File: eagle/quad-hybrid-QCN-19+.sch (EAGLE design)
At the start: 6 parts, among them J1 142-0701-851, J2 142-0701-851, J3 142-0701-851, U1 QCN-19D+

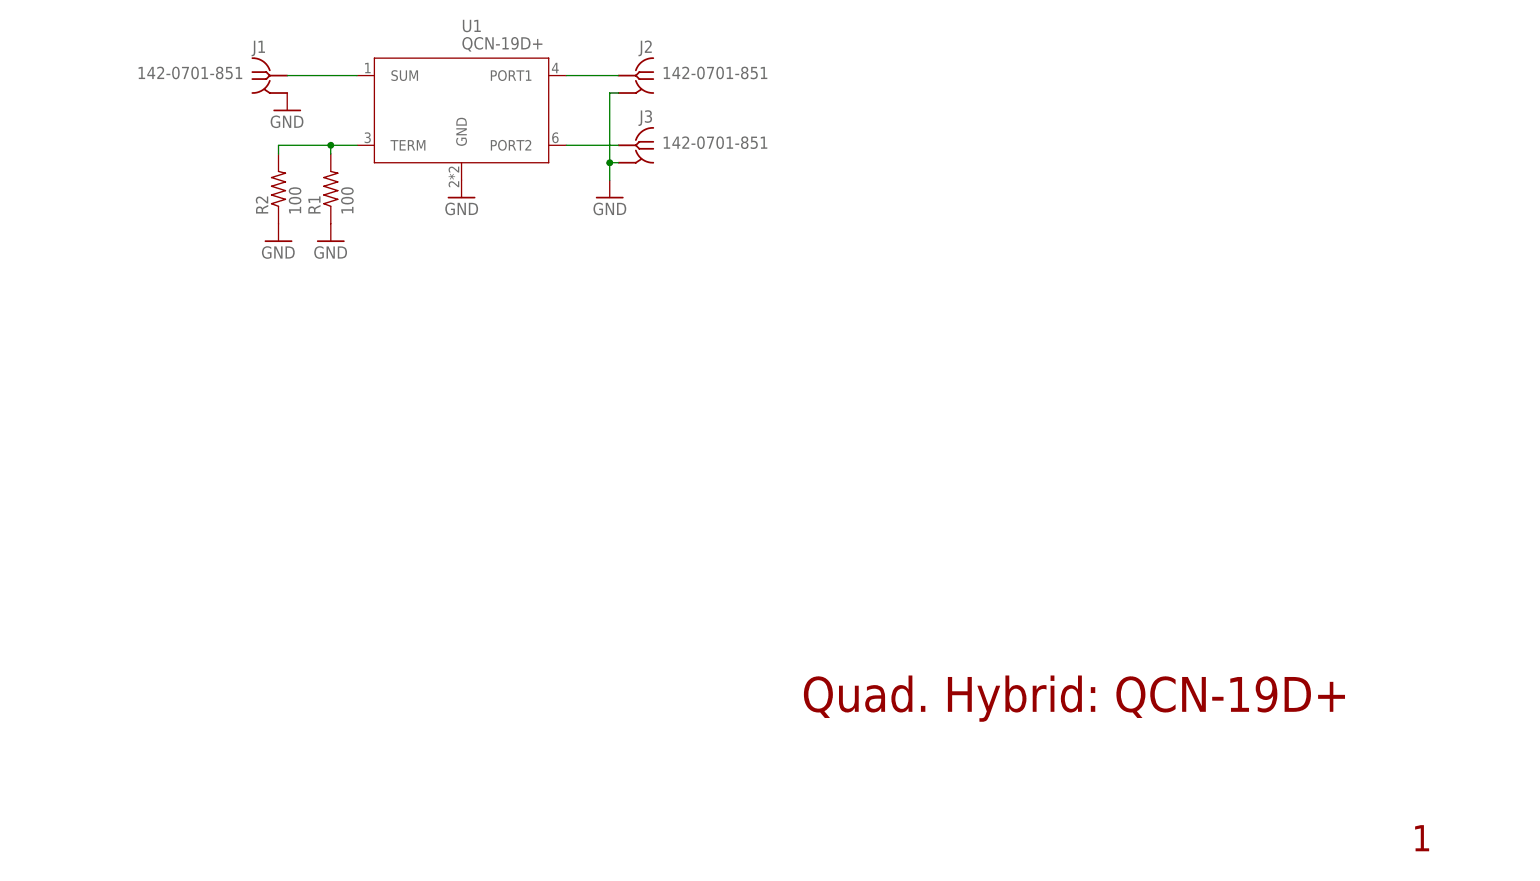
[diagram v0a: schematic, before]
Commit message: Update QCN-19+ names
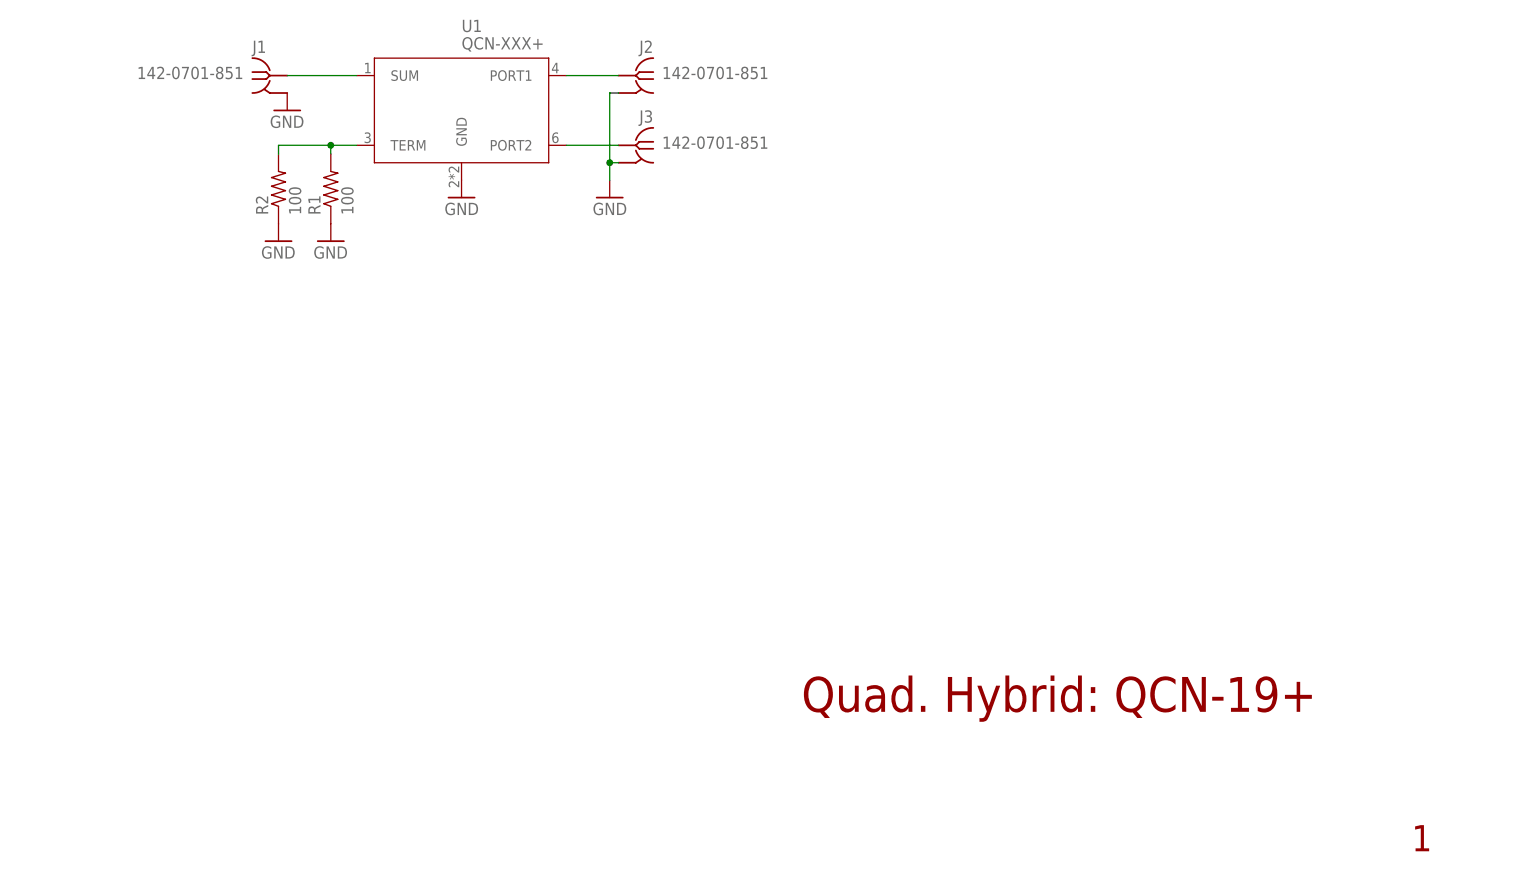
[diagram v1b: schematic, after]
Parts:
- U1: value QCN-19D+ -> QCN-XXX+; device U-MiniCirc-QCN-19+-quad:QCN-19D+ -> U-MiniCirc-QCN-XXX+-quad:QCN-XXX+
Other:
- note added: "Quad. Hybrid: QCN-19+"
- note removed: "Quad. Hybrid: QCN-19D+"
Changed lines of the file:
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@@
 <part name="GND3" library="supply1" library_urn="urn:adsk.eagle:library:371" deviceset="GND" device=""/>
 <part name="GND4" library="supply1" library_urn="urn:adsk.eagle:library:371" deviceset="GND" device=""/>
-<part name="U1" library="U-MiniCirc-QCN-19+-quad" deviceset="QCN-19D+" device=""/>
+<part name="U1" library="U-MiniCirc-QCN-XXX+-quad" deviceset="QCN-XXX+" device=""/>
 </parts>
 <sheets>
 <sheet>
 <plain>
-<text x="176.53" y="26.67" size="5.08" layer="94">Quad. Hybrid: QCN-19D+</text>
+<text x="176.53" y="26.67" size="5.08" layer="94">Quad. Hybrid: QCN-19+</text>
 <text x="265.43" y="6.35" size="3.81" layer="94">1</text>
 </plain>

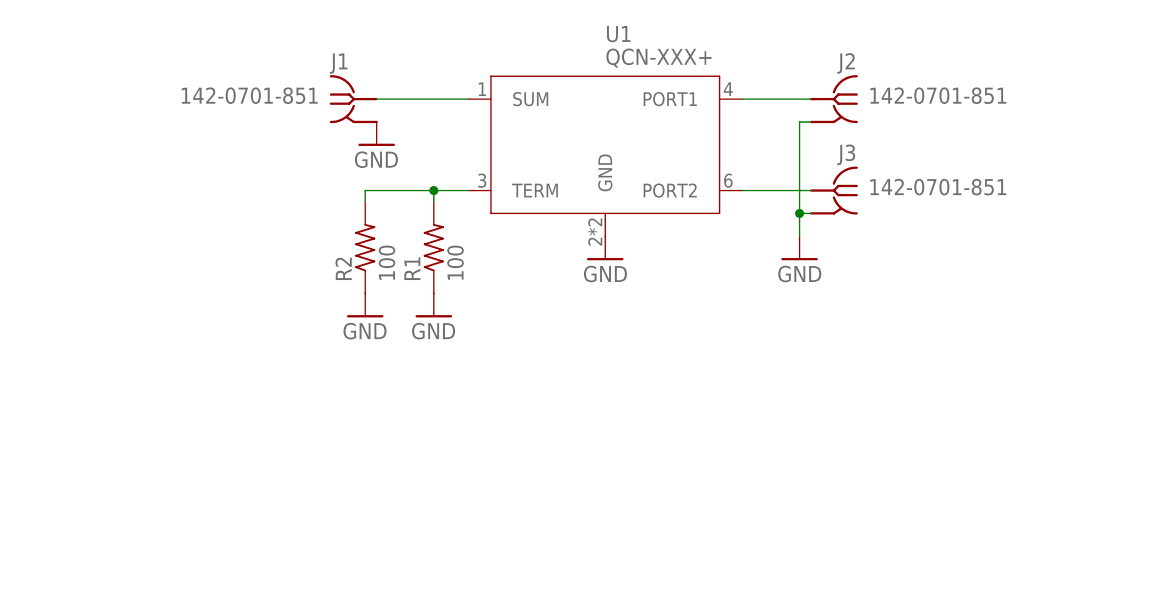
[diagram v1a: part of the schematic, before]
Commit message: Update QCN-19+, add optional isolation port
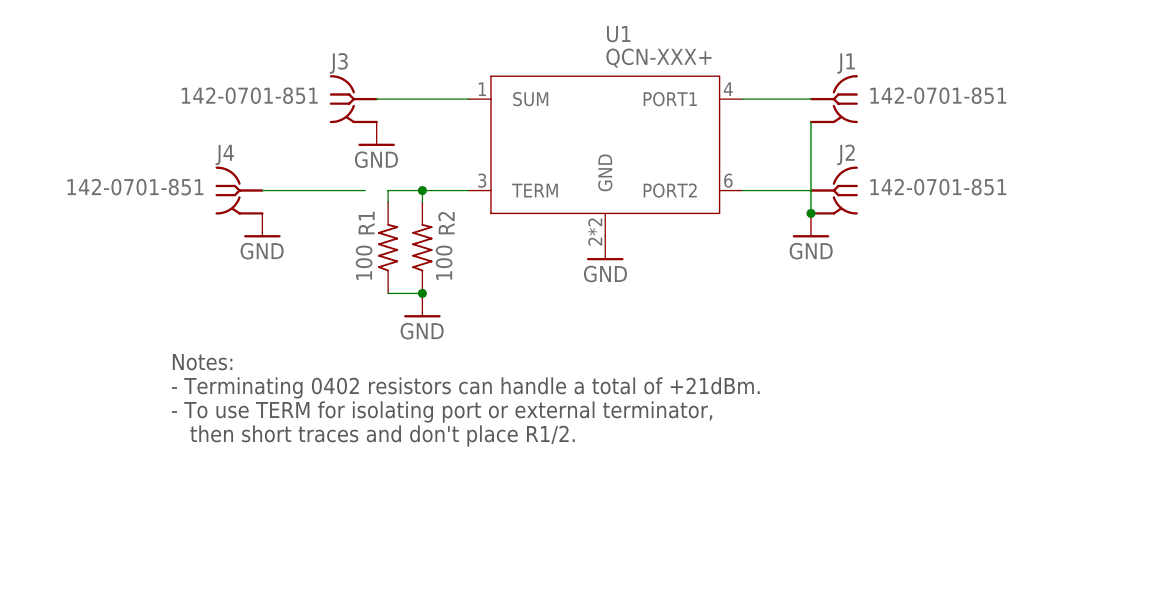
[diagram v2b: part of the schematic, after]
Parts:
- added J4: 142-0701-851, J-Cinch-142-0701-851-SMA-end-launch:142-0701-851
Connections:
- removed net PORT1: J2.RF, U1.PORT1
- removed net PORT2: J3.RF, U1.PORT2
- new net ISO: J4.RF
- new net P1: J1.RF, U1.PORT1
- new net P2: J2.RF, U1.PORT2
- net GND: now also J4.GND
- net SUM: now also J3.RF; no longer J1.RF
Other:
- note added: "Notes: - Terminating 0402 resistors can handle a total of +21dBm. - To use TERM for isolating port or external terminator, then short traces and don't place R1/2."
- moved on the sheet: J1, J2, J3, R1, R2
